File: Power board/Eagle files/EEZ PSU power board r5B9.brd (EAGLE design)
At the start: 150 x 74 mm, 276 parts, among them IC1 LTC3864EMSE#PBF, IC10 REF5025AIDG4, IC11 DAC8552IDGKTG4, IC12 ADG465SOT-23, IC13 TS5A9411DCKT, IC14 ADS1120IPWR, IC15 LP339D, IC2 MC79L05, IC3 MC78L05, IC4 LM5574MTX/NOPB, IC5 LP2951SO8, IC6 TL072D, IC7 TL072D, IC8 OP27GSZ, IC9 MCP23S08-E/SO, Q1 SUD19P06-60, Q10 MMBT5401, Q11 MMBT5401, Q12 MMBT5551, Q13 MMBT5551, Q14 BSS84P, Q15 2N7002, Q16 MMBT5551, Q17 MMBT5401, Q18 MMBT5551, Q19 MMBT5551, Q2 MMBT5401, Q3 2N7002, Q4 IRFP250N, Q5 BC857C, Q6 BC846C, Q7 BCP56-16.115, Q8 IRFR5410, Q9 BCP56-16.115, X1 39303035, X2 282836-2, X3 SSW-113-02-T-D-RA

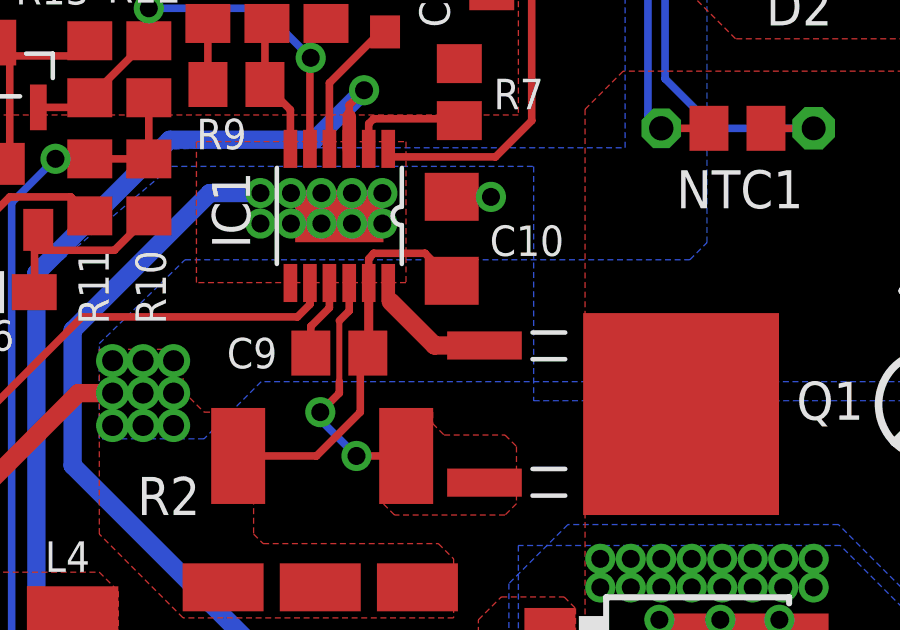
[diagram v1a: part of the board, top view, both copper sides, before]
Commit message: BOM corrections, Q1 gate trace improved
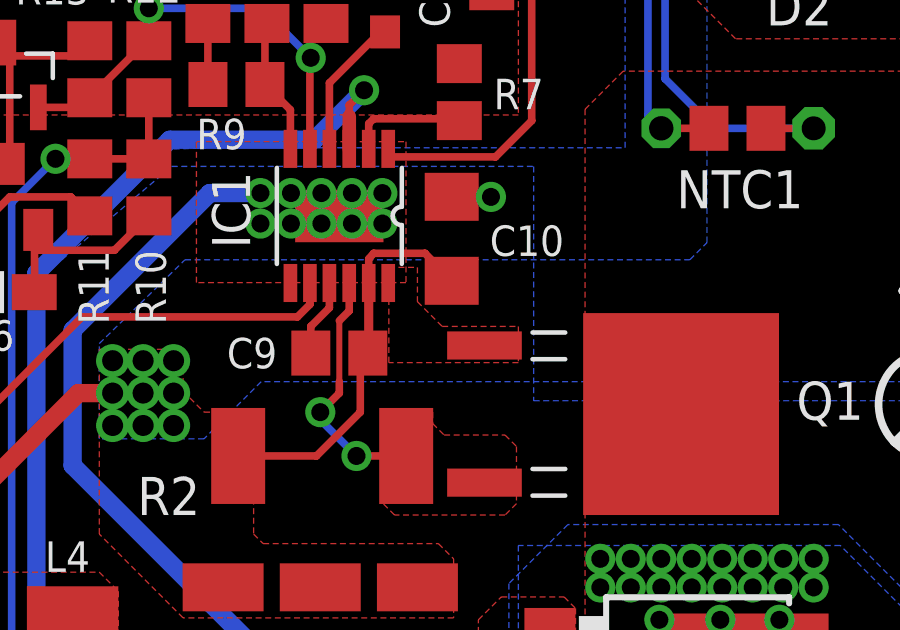
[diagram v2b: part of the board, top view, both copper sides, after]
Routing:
- net N$30: track 4.32 -> 0.00 mm
- added copper zone on layer 1, net N$30
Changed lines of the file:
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@@
 <layer number="113" name="dimension2" color="7" fill="1" visible="yes" active="yes"/>
 <layer number="114" name="custom" color="10" fill="1" visible="no" active="yes"/>
+<layer number="115" name="border" color="12" fill="1" visible="no" active="yes"/>
 <layer number="116" name="Patch_BOT" color="7" fill="1" visible="no" active="no"/>
+<layer number="117" name="bridges" color="10" fill="1" visible="no" active="yes"/>
 <layer number="118" name="Rect_Pads" color="7" fill="1" visible="no" active="no"/>
+<layer number="119" name="230VAC_spacing" color="11" fill="1" visible="no" active="yes"/>
 <layer number="121" name="_tsilk" color="7" fill="1" visible="no" active="no"/>
 <layer number="122" name="_bsilk" color="7" fill="1" visible="no" active="no"/>
@@
 <via x="107.2261" y="115.6335" extent="1-16" drill="0.6" shape="square"/>
 <via x="111.2901" y="115.6335" extent="1-16" drill="0.6" shape="square"/>
-<polygon width="0.254" layer="1" isolate="0.3048" thermals="no">
+<polygon width="0.254" layer="1" isolate="0.3048" thermals="no" rank="2">
 <vertex x="105.0925" y="118.364"/>
 <vertex x="112.0775" y="118.364"/>
@@
 <contactref element="Q1" pad="1"/>
 <contactref element="IC1" pad="12"/>
-<wire x1="111.485" y1="113.6523" x2="111.485" y2="113.178" width="0.254" layer="1"/>
-<wire x1="111.485" y1="113.178" x2="111.5695" y2="113.0935" width="0.254" layer="1"/>
-<wire x1="114.6937" y1="111.5695" x2="113.03" y2="111.5695" width="0.6096" layer="1"/>
-<wire x1="111.5695" y1="113.03" x2="113.03" y2="111.5695" width="0.6096" layer="1"/>
-<wire x1="111.5695" y1="113.03" x2="111.5695" y2="113.0935" width="0" layer="19" extent="1-1"/>
+<polygon width="0.254" layer="1" isolate="0.3048" thermals="no">
+<vertex x="111.506" y="114.173"/>
+<vertex x="112.4585" y="114.173"/>
+<vertex x="112.4585" y="113.03"/>
+<vertex x="113.284" y="112.2045"/>
+<vertex x="115.824" y="112.2045"/>
+<vertex x="115.824" y="110.998"/>
+<vertex x="111.506" y="110.998"/>
+</polygon>
 </signal>
 <signal name="N$31">

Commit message: C39 marked as n.c.
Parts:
- C39: value 2u2 -> n.c.
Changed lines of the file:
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@@
 <attribute name="VALUE" x="105.537" y="133.35" size="0.8128" layer="27" ratio="10" rot="R270"/>
 </element>
-<element name="C39" library="rcl" package="C0805" value="2u2" x="98.298" y="129.54" smashed="yes" rot="R270">
+<element name="C39" library="rcl" package="C0805" value="n.c." x="98.298" y="129.54" smashed="yes" rot="R270">
 <attribute name="NAME" x="97.917" y="127.1905" size="1.016" layer="25" ratio="10" rot="R270"/>
 <attribute name="VALUE" x="98.679" y="128.397" size="1.016" layer="27" ratio="10" rot="R90"/>

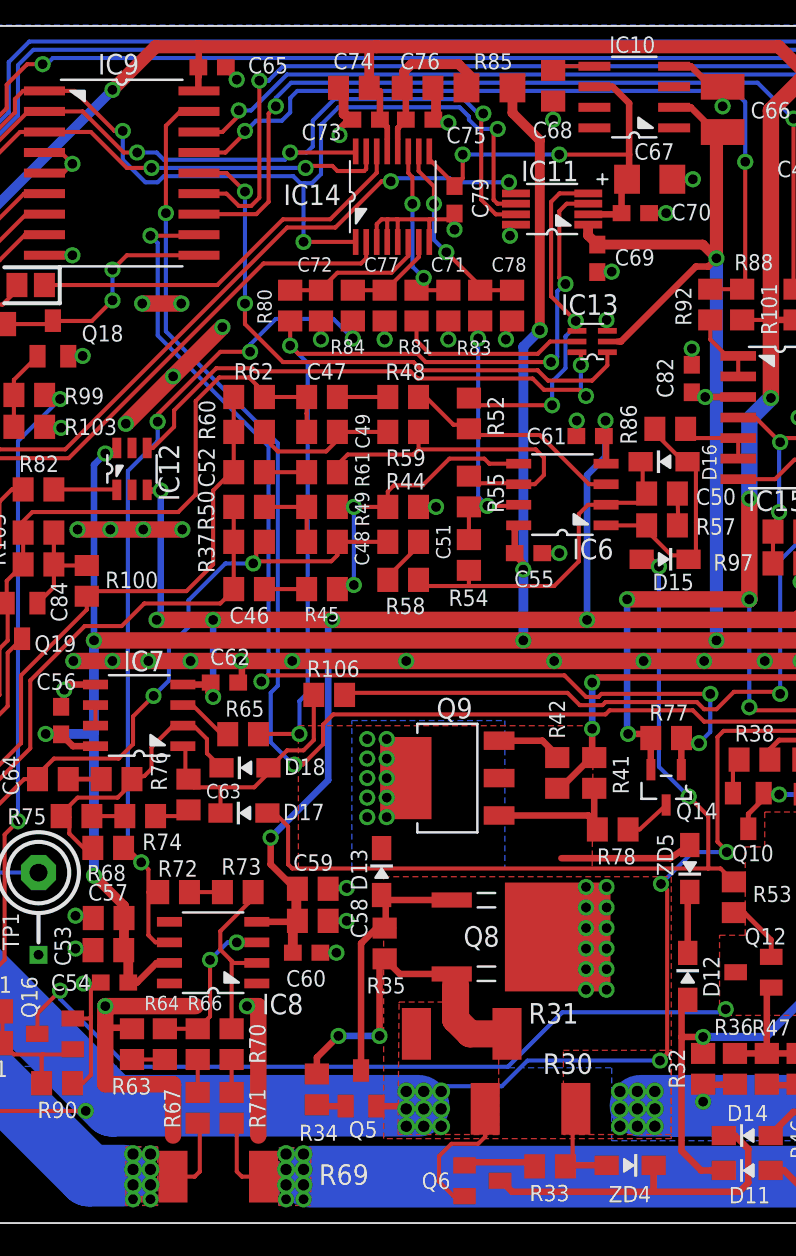
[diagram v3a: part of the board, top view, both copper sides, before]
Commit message: Small corrections on top silkscreen
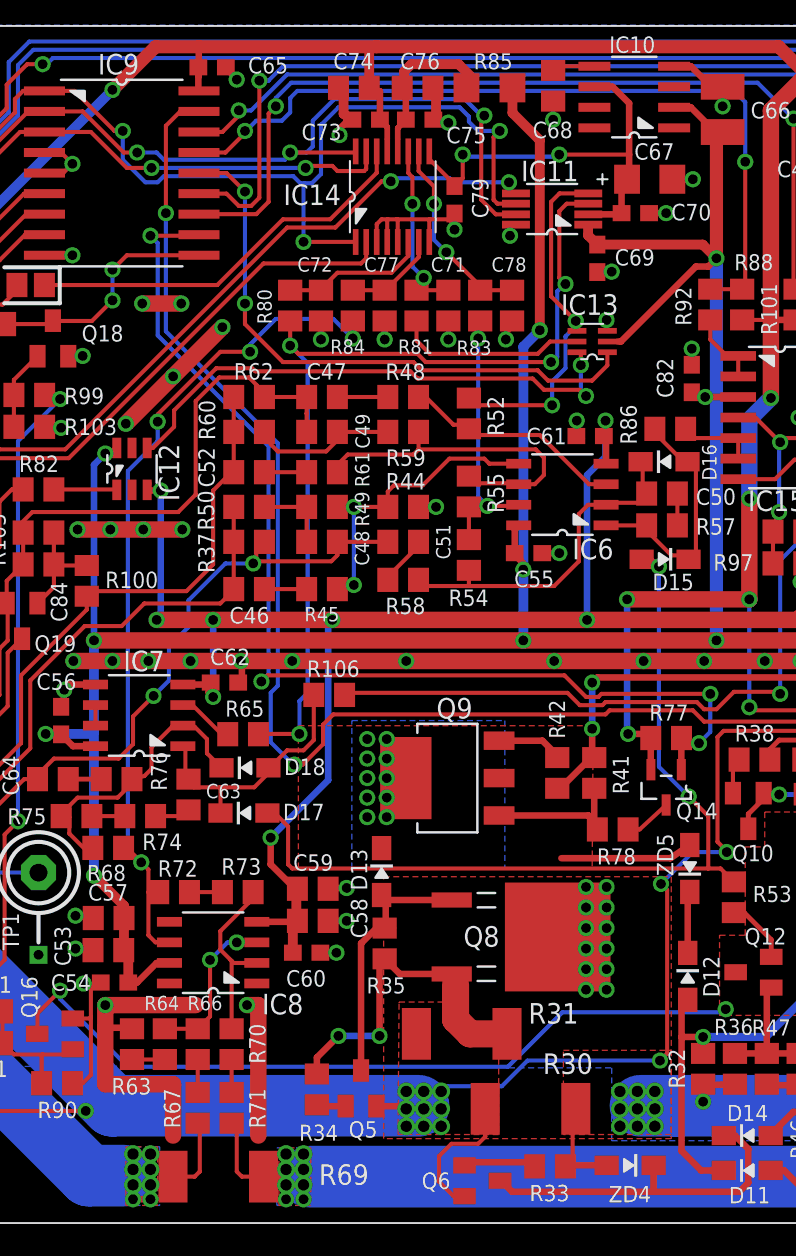
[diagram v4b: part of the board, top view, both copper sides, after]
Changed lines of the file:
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@@
 <wire x1="18.3515" y1="93.1545" x2="28.194" y2="83.312" width="2.54" layer="30"/>
 <wire x1="28.194" y1="83.312" x2="45.9105" y2="83.312" width="2.54" layer="30"/>
-<wire x1="39.1795" y1="78.867" x2="98.044" y2="78.867" width="2.54" layer="30"/>
+<wire x1="39.624" y1="78.867" x2="98.044" y2="78.867" width="2.54" layer="30"/>
 <wire x1="98.044" y1="78.867" x2="109.728" y2="90.551" width="2.54" layer="30"/>
 <wire x1="109.728" y1="90.551" x2="109.728" y2="95.504" width="2.54" layer="30"/>
@@
 <contactref element="Q8" pad="2"/>
 <contactref element="C44" pad="2"/>
-<via x="27.686" y="89.408" extent="1-16" drill="0.6" shape="square"/>
+<via x="27.686" y="89.4715" extent="1-16" drill="0.6" shape="square"/>
 <wire x1="26.896" y1="92.964" x2="26.9265" y2="92.87" width="0.4064" layer="1"/>
 <via x="42.6075" y="96.7115" extent="1-16" drill="0.6" shape="square"/>
@@
 <wire x1="90.297" y1="90.3605" x2="90.297" y2="91.57" width="0.4064" layer="1"/>
 <wire x1="90.297" y1="91.57" x2="90.173" y2="91.694" width="0.4064" layer="1"/>
-<wire x1="37.1475" y1="81.407" x2="37.1475" y2="89.408" width="1.016" layer="1"/>
+<wire x1="37.1475" y1="81.407" x2="37.1475" y2="89.4715" width="1.016" layer="1"/>
 <wire x1="27.686" y1="84.582" x2="27.686" y2="88.0745" width="1.016" layer="1"/>
-<wire x1="27.686" y1="88.0745" x2="27.686" y2="89.408" width="1.016" layer="1"/>
+<wire x1="27.686" y1="88.0745" x2="27.686" y2="89.4715" width="1.016" layer="1"/>
 <wire x1="29.4005" y1="88.072" x2="27.6885" y2="88.072" width="0.4064" layer="1"/>
 <wire x1="27.6885" y1="88.072" x2="27.686" y2="88.0745" width="0.4064" layer="1"/>
@@
 <wire x1="26.797" y1="88.7095" x2="26.797" y2="90.6891625" width="0.254" layer="1"/>
 <wire x1="26.797" y1="90.6891625" x2="26.890796875" y2="90.782959375" width="0.254" layer="1"/>
-<wire x1="33.274" y1="89.408" x2="27.686" y2="89.408" width="1.016" layer="1"/>
-<wire x1="37.1475" y1="89.408" x2="36.449" y2="89.408" width="1.016" layer="1"/>
-<via x="36.449" y="89.408" extent="1-16" drill="0.6" shape="square"/>
+<wire x1="33.274" y1="89.4715" x2="27.686" y2="89.4715" width="1.016" layer="1"/>
+<wire x1="37.1475" y1="89.4715" x2="36.449" y2="89.4715" width="1.016" layer="1"/>
+<via x="36.449" y="89.4715" extent="1-16" drill="0.6" shape="square"/>
 <wire x1="88.607" y1="115.1255" x2="88.607" y2="116.752" width="0.4064" layer="1"/>
 <wire x1="88.607" y1="116.752" x2="88.0745" y2="117.2845" width="0.4064" layer="1"/>
@@
 <wire x1="63.68" y1="123.063" x2="63.807" y2="123.1265" width="0.254" layer="1"/>
 <wire x1="63.807" y1="123.1265" x2="63.8705" y2="123.1265" width="0.254" layer="1"/>
-<wire x1="64.1985" y1="123.1265" x2="64.1985" y2="119.3165" width="0.254" layer="1"/>
-<wire x1="64.1985" y1="119.3165" x2="64.1985" y2="117.094" width="0.254" layer="1"/>
+<wire x1="64.1985" y1="123.1265" x2="64.1985" y2="117.094" width="0.254" layer="1"/>
 <wire x1="64.1985" y1="117.094" x2="64.0715" y2="117.094" width="0.254" layer="1"/>
 <wire x1="64.0715" y1="117.094" x2="64.0715" y2="117.0305" width="0.254" layer="1"/>
 <wire x1="64.0715" y1="117.0305" x2="63.7435" y2="117.0305" width="0.254" layer="1"/>
 <wire x1="64.188" y1="122.682" x2="63.68" y2="123.063" width="0.254" layer="1"/>
-<wire x1="64.262" y1="119.253" x2="64.1985" y2="119.3165" width="0.254" layer="1"/>
 <wire x1="59.2455" y1="119.126" x2="61.153" y2="119.126" width="0.254" layer="1"/>
 <wire x1="63.68" y1="123.063" x2="63.4365" y2="123.063" width="0.254" layer="1"/>
@@
 <wire x1="39.9415" y1="136.652" x2="43.16" y2="136.652" width="0.254" layer="1"/>
 <wire x1="43.16" y1="136.652" x2="43.166" y2="136.646" width="0.254" layer="1"/>
-<via x="51.943" y="143.637" extent="1-16" drill="0.6" shape="octagon"/>
+<via x="52.07" y="143.51" extent="1-16" drill="0.6" shape="octagon"/>
 <wire x1="53.0733" y1="139.0142" x2="51.9303" y2="139.0142" width="0.254" layer="1"/>
 <wire x1="51.9303" y1="139.0142" x2="51.689" y2="139.2555" width="0.254" layer="1"/>
-<wire x1="51.689" y1="139.2555" x2="51.689" y2="143.4465" width="0.254" layer="1"/>
-<wire x1="51.689" y1="143.4465" x2="51.943" y2="143.637" width="0.254" layer="1"/>
+<wire x1="51.689" y1="139.2555" x2="51.689" y2="143.129" width="0.254" layer="1"/>
+<wire x1="51.689" y1="143.129" x2="52.07" y2="143.51" width="0.254" layer="1"/>
 <wire x1="49.5935" y1="144.9705" x2="50.165" y2="144.399" width="0.254" layer="16"/>
-<wire x1="50.165" y1="144.399" x2="50.165" y2="144.2085" width="0.254" layer="16"/>
-<wire x1="50.165" y1="144.2085" x2="50.7365" y2="143.637" width="0.254" layer="16"/>
-<wire x1="50.7365" y1="143.637" x2="51.943" y2="143.637" width="0.254" layer="16"/>
 <wire x1="31.3055" y1="140.716" x2="39.3065" y2="140.716" width="0.254" layer="16"/>
 <wire x1="39.3065" y1="140.716" x2="39.751" y2="140.2715" width="0.254" layer="16"/>
@@
 <wire x1="39.9415" y1="136.652" x2="39.9415" y2="140.208" width="0.254" layer="16"/>
 <wire x1="39.9415" y1="140.208" x2="40.005" y2="140.2715" width="0.254" layer="16"/>
+<wire x1="50.165" y1="144.399" x2="50.165" y2="144.0815" width="0.254" layer="16"/>
+<wire x1="50.165" y1="144.0815" x2="50.7365" y2="143.51" width="0.254" layer="16"/>
+<wire x1="50.7365" y1="143.51" x2="52.07" y2="143.51" width="0.254" layer="16"/>
 </signal>
 <signal name="PS_MOSI">
@@
 <wire x1="31.3055" y1="141.732" x2="38.7985" y2="141.732" width="0.254" layer="16"/>
 <wire x1="38.7985" y1="141.732" x2="39.116" y2="142.1765" width="0.254" layer="16"/>
-<wire x1="41.8465" y1="145.4785" x2="49.8475" y2="145.4785" width="0.254" layer="16"/>
-<via x="51.054" y="144.5895" extent="1-16" drill="0.6" shape="octagon"/>
+<wire x1="41.8465" y1="145.4785" x2="49.911" y2="145.4785" width="0.254" layer="16"/>
+<via x="51.1175" y="144.4625" extent="1-16" drill="0.6" shape="octagon"/>
 <wire x1="53.0733" y1="138.3538" x2="51.8287" y2="138.3538" width="0.254" layer="1"/>
 <wire x1="51.8287" y1="138.3538" x2="50.927" y2="139.2555" width="0.254" layer="1"/>
-<wire x1="50.927" y1="139.2555" x2="50.927" y2="144.4625" width="0.254" layer="1"/>
-<wire x1="51.054" y1="144.5895" x2="50.7365" y2="144.5895" width="0.254" layer="16"/>
-<wire x1="50.7365" y1="144.5895" x2="49.8475" y2="145.4785" width="0.254" layer="16"/>
-<wire x1="50.927" y1="144.4625" x2="51.054" y2="144.5895" width="0.254" layer="1"/>
+<wire x1="50.927" y1="139.2555" x2="50.927" y2="144.272" width="0.254" layer="1"/>
 <wire x1="41.8465" y1="145.4785" x2="40.513" y2="144.145" width="0.254" layer="16"/>
 <wire x1="39.116" y1="142.1765" x2="43.0965" y2="142.1765" width="0.254" layer="1"/>
@@
 <wire x1="16.972" y1="128.31" x2="16.972" y2="130.9545" width="0.254" layer="1"/>
 <wire x1="16.972" y1="130.9545" x2="17.018" y2="131.0005" width="0.254" layer="1"/>
+<wire x1="51.1175" y1="144.4625" x2="50.927" y2="144.4625" width="0.254" layer="16"/>
+<wire x1="50.927" y1="144.4625" x2="49.911" y2="145.4785" width="0.254" layer="16"/>
+<wire x1="50.927" y1="144.272" x2="51.1175" y2="144.4625" width="0.254" layer="1"/>
 </signal>
 <signal name="CS_DAC">
@@
 <wire x1="47.752" y1="142.21" x2="47.716" y2="142.246" width="0.254" layer="1"/>
 <via x="49.784" y="142.0495" extent="1-16" drill="0.6" shape="octagon"/>
-<wire x1="49.784" y1="142.0495" x2="55.753" y2="142.0495" width="0.254" layer="16"/>
 <via x="55.753" y="142.0495" extent="1-16" drill="0.6" shape="octagon"/>
 <wire x1="60.071" y1="145.2245" x2="59.055" y2="146.2405" width="0.4064" layer="1"/>
@@
 <wire x1="60.071" y1="140.586" x2="59.941" y2="140.5255" width="0.4064" layer="1"/>
 <wire x1="55.753" y1="142.0495" x2="60.071" y2="142.0495" width="0.254" layer="1"/>
+<wire x1="55.753" y1="142.0495" x2="55.626" y2="141.9225" width="0.254" layer="16"/>
+<wire x1="55.626" y1="141.9225" x2="49.911" y2="141.9225" width="0.254" layer="16"/>
+<wire x1="49.911" y1="141.9225" x2="49.784" y2="142.0495" width="0.254" layer="16"/>
 <wire x1="49.276" y1="140.1055" x2="49.276" y2="140.081" width="0" layer="19" extent="1-1"/>
 </signal>
@@
 </polygon>
 <polygon width="0.254" layer="16" isolate="0.3048" thermals="no">
-<vertex x="30.9245" y="80.7085"/>
-<vertex x="30.9245" y="77.089"/>
+<vertex x="31.0515" y="80.7085"/>
+<vertex x="31.0515" y="77.089"/>
 <vertex x="28.956" y="77.089"/>
 <vertex x="28.956" y="80.7085"/>
@@
 <vertex x="40.386" y="80.645"/>
 <vertex x="40.386" y="77.089"/>
-<vertex x="38.4175" y="77.089"/>
-<vertex x="38.4175" y="80.645"/>
+<vertex x="38.2905" y="77.089"/>
+<vertex x="38.2905" y="80.645"/>
 </polygon>
 <contactref element="C16" pad="2"/>
@@
 <contactref element="C50" pad="2"/>
 <contactref element="R57" pad="1"/>
-<wire x1="63.053" y1="121.0945" x2="63.1165" y2="119.187" width="0.254" layer="1"/>
-<wire x1="63.1165" y1="119.187" x2="63.0555" y2="119.126" width="0.254" layer="1"/>
-<wire x1="63.0555" y1="119.126" x2="63.053" y2="119.126" width="0" layer="19" extent="1-1"/>
+<wire x1="63.053" y1="121.0945" x2="63.053" y2="119.126" width="0.254" layer="1"/>
 </signal>
 <signal name="INV_GND1">
@@
 </signal>
 </signals>
+<errors>
+</errors>
 </board>
 </drawing>

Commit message: R97 and R102 values swapped
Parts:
- R102: value 5K6 -> 4K7
- R97: value 4K7 -> 5K6
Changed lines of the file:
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@@
 <attribute name="VALUE" x="45.4025" y="144.7165" size="1.016" layer="27" ratio="10" rot="R180"/>
 </element>
-<element name="R102" library="rcl" package="R0805" value="5K6" x="69.9135" y="118.745" smashed="yes" rot="R180">
+<element name="R102" library="rcl" package="R0805" value="4K7" x="69.9135" y="118.745" smashed="yes" rot="R180">
 <attribute name="NAME" x="72.0344" y="118.3259" size="1.016" layer="25" ratio="10"/>
 <attribute name="VALUE" x="68.6054" y="118.2751" size="1.016" layer="27" ratio="10"/>
@@
 <attribute name="VALUE" x="86.6775" y="91.059" size="1.016" layer="27" ratio="10"/>
 </element>
-<element name="R97" library="rcl" package="R0805" value="4K7" x="69.9135" y="116.7765" smashed="yes">
+<element name="R97" library="rcl" package="R0805" value="5K6" x="69.9135" y="116.7765" smashed="yes">
 <attribute name="NAME" x="65.278" y="116.332" size="1.016" layer="25" ratio="10"/>
 <attribute name="VALUE" x="68.3895" y="116.0145" size="1.016" layer="27" ratio="10"/>
@@
 </signal>
 </signals>
-<errors>
-</errors>
 </board>
 </drawing>
